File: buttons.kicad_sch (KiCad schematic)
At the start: 0 parts

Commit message: Added oled hierarchical page and referenced other pages
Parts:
- added C? (x14): 100nf, symbol Device:C_Small
- added R? (x14): 10k, Resistor_SMD:R_0201_0603Metric, symbol Device:R
- added SW?: sw_8, ksoloti_shield_footprints:TL1105T, symbol ksoloti_shield_symbols:TL1105_tact_switch_6mm
- added SW?: sw_7, ksoloti_shield_footprints:TL1105T, symbol ksoloti_shield_symbols:TL1105_tact_switch_6mm
- added SW?: sw_c, ksoloti_shield_footprints:TL1105T, symbol ksoloti_shield_symbols:TL1105_tact_switch_6mm
- added SW?: sw_4, ksoloti_shield_footprints:TL1105T, symbol ksoloti_shield_symbols:TL1105_tact_switch_6mm
- added SW?: sw_3, ksoloti_shield_footprints:TL1105T, symbol ksoloti_shield_symbols:TL1105_tact_switch_6mm
- added SW?: sw_b, ksoloti_shield_footprints:TL1105T, symbol ksoloti_shield_symbols:TL1105_tact_switch_6mm
- added SW?: sw_6, ksoloti_shield_footprints:TL1105T, symbol ksoloti_shield_symbols:TL1105_tact_switch_6mm
- added SW?: sw_2, ksoloti_shield_footprints:TL1105T, symbol ksoloti_shield_symbols:TL1105_tact_switch_6mm
- added SW?: sw_1, ksoloti_shield_footprints:TL1105T, symbol ksoloti_shield_symbols:TL1105_tact_switch_6mm
- added SW?: sw_a, ksoloti_shield_footprints:TL1105T, symbol ksoloti_shield_symbols:TL1105_tact_switch_6mm
- added SW?: sw_d, ksoloti_shield_footprints:TL1105T, symbol ksoloti_shield_symbols:TL1105_tact_switch_6mm
- added SW?: sw_5, ksoloti_shield_footprints:TL1105T, symbol ksoloti_shield_symbols:TL1105_tact_switch_6mm
- added SW?: back, ksoloti_shield_footprints:TL1105T, symbol ksoloti_shield_symbols:TL1105_tact_switch_6mm
- added SW?: system, ksoloti_shield_footprints:TL1105T, symbol ksoloti_shield_symbols:TL1105_tact_switch_6mm
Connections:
- new net +3.3V: R?.2, R?.2, R?.2, R?.2, R?.2, R?.2, R?.2, R?.2, R?.2, R?.2, R?.2, R?.2, R?.2, R?.2
- new net GND: C?.2, C?.2, C?.2, C?.2, C?.2, C?.2, C?.2, C?.2, C?.2, C?.2, C?.2, C?.2, C?.2, C?.2, SW?.1, SW?.1, SW?.1, SW?.1, SW?.1, SW?.1, SW?.1, SW?.1, SW?.1, SW?.1, SW?.1, SW?.1, SW?.1, SW?.1
- new net SW_1: C?.1, R?.1, SW?.3
- new net SW_2: C?.1, R?.1, SW?.3
- new net SW_3: C?.1, R?.1, SW?.3
- new net SW_4: C?.1, R?.1, SW?.3
- new net SW_5: C?.1, R?.1, SW?.3
- new net SW_6: C?.1, R?.1, SW?.3
- new net SW_7: C?.1, R?.1, SW?.3
- new net SW_8: C?.1, R?.1, SW?.3
- new net SW_A: C?.1, R?.1, SW?.3
- new net SW_B: C?.1, R?.1, SW?.3
- new net SW_BACK: C?.1, R?.1, SW?.3
- new net SW_C: C?.1, R?.1, SW?.3
- new net SW_D: C?.1, R?.1, SW?.3
- new net SW_SYSTEM: C?.1, R?.1, SW?.3

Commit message: Annotated all components (numerating)
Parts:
- gave numbers to parts that had none: 42

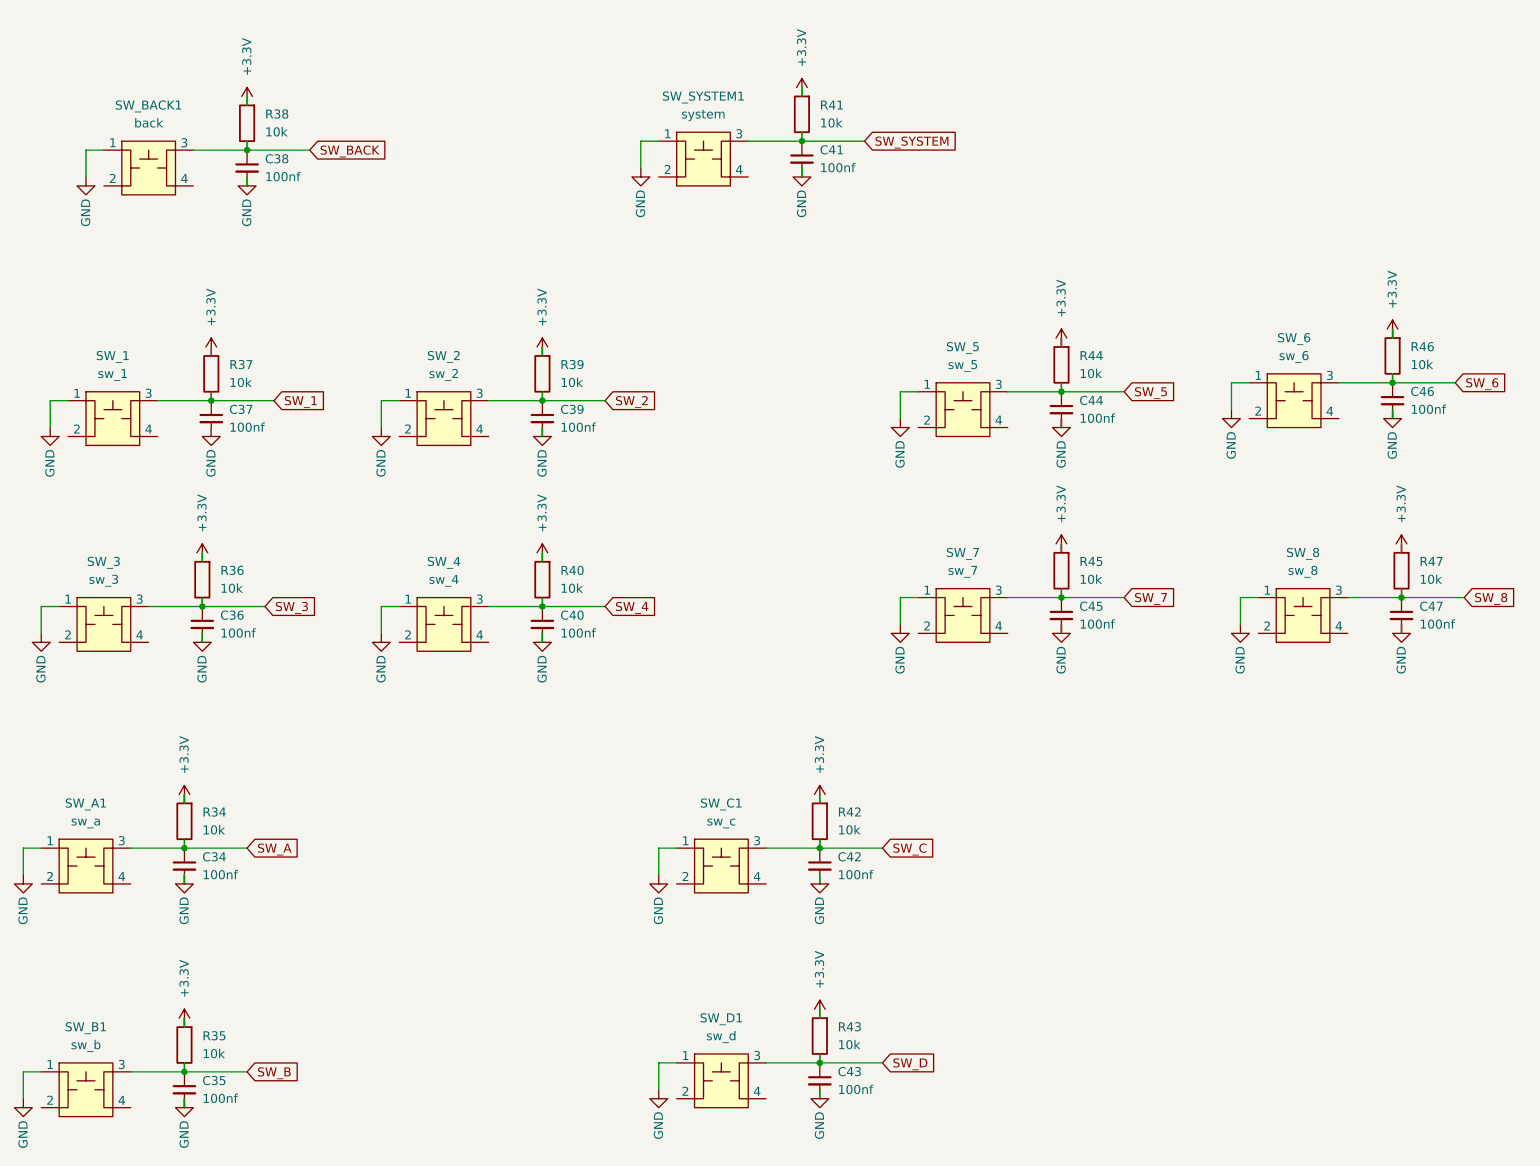
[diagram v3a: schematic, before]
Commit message: Cleaned up ERC errors
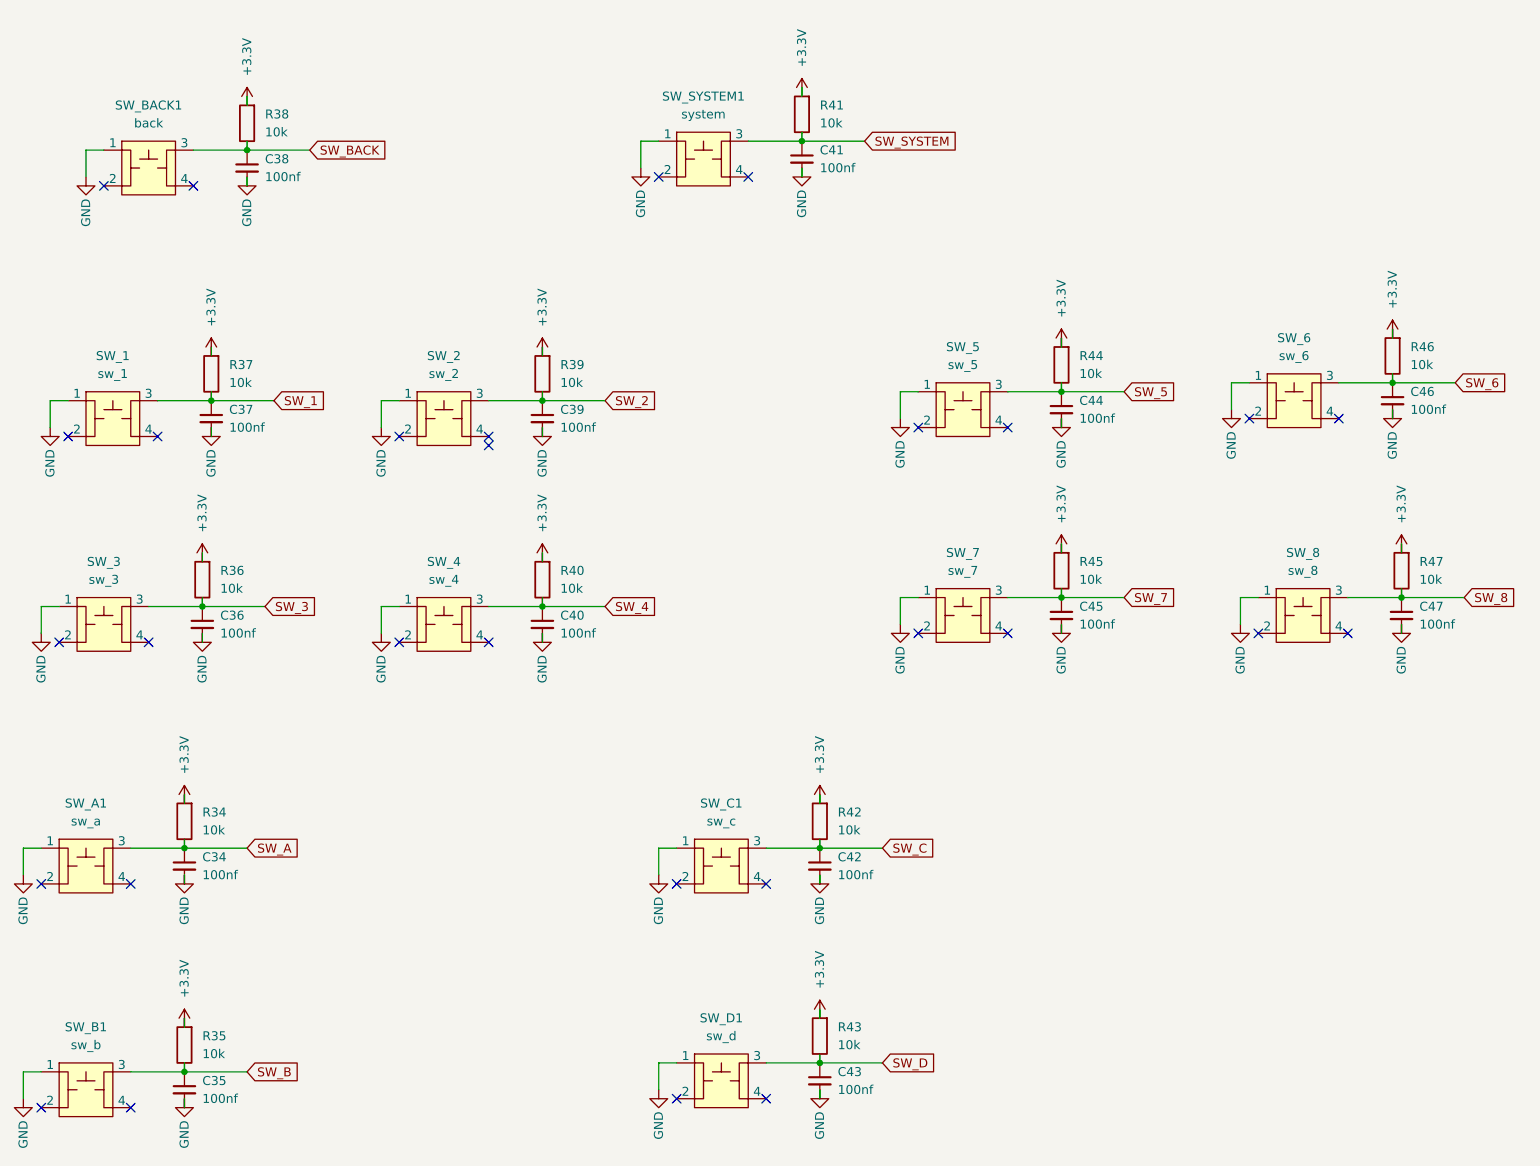
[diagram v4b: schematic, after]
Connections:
- no-connect marks 0 -> 29
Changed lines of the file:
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@@
 		(color 0 0 0 0)
+	)
+	(no_connect
+		(at 46.99 73.66)
+	)
+	(no_connect
+		(at 214.63 71.12)
+	)
+	(no_connect
+		(at 43.18 168.91)
+	)
+	(no_connect
+		(at 154.94 72.39)
+	)
+	(no_connect
+		(at 133.35 167.64)
+	)
+	(no_connect
+		(at 167.64 72.39)
+	)
+	(no_connect
+		(at 45.72 102.87)
+	)
+	(no_connect
+		(at 154.94 101.6)
+	)
+	(no_connect
+		(at 93.98 102.87)
+	)
+	(no_connect
+		(at 118.11 36.83)
+	)
+	(no_connect
+		(at 52.07 38.1)
+	)
+	(no_connect
+		(at 130.81 36.83)
+	)
+	(no_connect
+		(at 201.93 71.12)
+	)
+	(no_connect
+		(at 33.02 102.87)
+	)
+	(no_connect
+		(at 30.48 137.16)
+	)
+	(no_connect
+		(at 93.98 73.66)
+	)
+	(no_connect
+		(at 133.35 137.16)
+	)
+	(no_connect
+		(at 203.2 101.6)
+	)
+	(no_connect
+		(at 167.64 101.6)
+	)
+	(no_connect
+		(at 81.28 73.66)
+	)
+	(no_connect
+		(at 34.29 73.66)
+	)
+	(no_connect
+		(at 43.18 137.16)
+	)
+	(no_connect
+		(at 93.98 74.93)
+	)
+	(no_connect
+		(at 81.28 102.87)
+	)
+	(no_connect
+		(at 215.9 101.6)
+	)
+	(no_connect
+		(at 120.65 167.64)
+	)
+	(no_connect
+		(at 39.37 38.1)
+	)
+	(no_connect
+		(at 30.48 168.91)
+	)
+	(no_connect
+		(at 120.65 137.16)
 	)
 	(wire

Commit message: Solve all warnings
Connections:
- no-connect marks 29 -> 28
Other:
- moved on the sheet: R34, R35, R36, R37, R38, R39, R40, R41, R42, R43, R44, R45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

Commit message: Added jack symbols and footprints also footprints for ics and caps
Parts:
- C34, C35, C36, C37, C38, C39, C40, C41, C42, C43, C44, C45, C46, C47: footprint (none) -> Capacitor_SMD:C_0603_1608Metric
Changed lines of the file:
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@@
 			)
 		)
-		(property "Footprint" ""
+		(property "Footprint" "Capacitor_SMD:C_0603_1608Metric"
 			(at 50.8 166.37 0)
 			(effects
@@
 			)
 		)
-		(property "Footprint" ""
+		(property "Footprint" "Capacitor_SMD:C_0603_1608Metric"
 			(at 101.6 100.33 0)
 			(effects
@@
 			)
 		)
-		(property "Footprint" ""
+		(property "Footprint" "Capacitor_SMD:C_0603_1608Metric"
 			(at 50.8 134.62 0)
 			(effects
@@
 			)
 		)
-		(property "Footprint" ""
+		(property "Footprint" "Capacitor_SMD:C_0603_1608Metric"
 			(at 175.26 69.85 0)
 			(effects
@@
 			)
 		)
-		(property "Footprint" ""
+		(property "Footprint" "Capacitor_SMD:C_0603_1608Metric"
 			(at 140.97 134.62 0)
 			(effects
@@
 			)
 		)
-		(property "Footprint" ""
+		(property "Footprint" "Capacitor_SMD:C_0603_1608Metric"
 			(at 175.26 99.06 0)
 			(effects
@@
 			)
 		)
-		(property "Footprint" ""
+		(property "Footprint" "Capacitor_SMD:C_0603_1608Metric"
 			(at 222.25 68.58 0)
 			(effects
@@
 			)
 		)
-		(property "Footprint" ""
+		(property "Footprint" "Capacitor_SMD:C_0603_1608Metric"
 			(at 53.34 100.33 0)
 			(effects
@@
 			)
 		)
-		(property "Footprint" ""
+		(property "Footprint" "Capacitor_SMD:C_0603_1608Metric"
 			(at 140.97 165.1 0)
 			(effects
@@
 			)
 		)
-		(property "Footprint" ""
+		(property "Footprint" "Capacitor_SMD:C_0603_1608Metric"
 			(at 59.69 35.56 0)
 			(effects
@@
 			)
 		)
-		(property "Footprint" ""
+		(property "Footprint" "Capacitor_SMD:C_0603_1608Metric"
 			(at 101.6 71.12 0)
 			(effects
@@
 			)
 		)
-		(property "Footprint" ""
+		(property "Footprint" "Capacitor_SMD:C_0603_1608Metric"
 			(at 138.43 34.29 0)
 			(effects
@@
 			)
 		)
-		(property "Footprint" ""
+		(property "Footprint" "Capacitor_SMD:C_0603_1608Metric"
 			(at 223.52 99.06 0)
 			(effects
@@
 			)
 		)
-		(property "Footprint" ""
+		(property "Footprint" "Capacitor_SMD:C_0603_1608Metric"
 			(at 54.61 71.12 0)
 			(effects
